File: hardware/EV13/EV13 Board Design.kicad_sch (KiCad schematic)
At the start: 142 parts, among them CN2 Conn_05x02_Female, CN3 Conn_01x06_Female, CN4 Conn_01x06_Female, CN5 Conn_02x05_Male, CN6 Conn_02x05_Male, CN7 Conn_02x05_Male, J1 Conn_01x02_Socket, J10 Conn_01x08_Socket, J2 AudioJack1, J3 Conn_01x06_Socket, J9 USB_C_Receptacle, SW1 TS-1037-A11B3-D2, SW3 TS-1037-A11B3-D2, SW4 SW_Push, SW5 SW_Push, SW6 SW_SPDT, U1 STM32F405RGTx, U11 ESP32-S3-WROOM-1-N8R2, U13 BM14B(0.8)-24DS-0.4V(53), U2 BQ21040DBV, U3 CH340C, U4 USBLC6-2P6, U5 M24C02-RMN6TP, U6 WM8960CGEFL/RV, U7 TPS63060, U8 STM32F072CBTx, Y1 Crystal_GND24

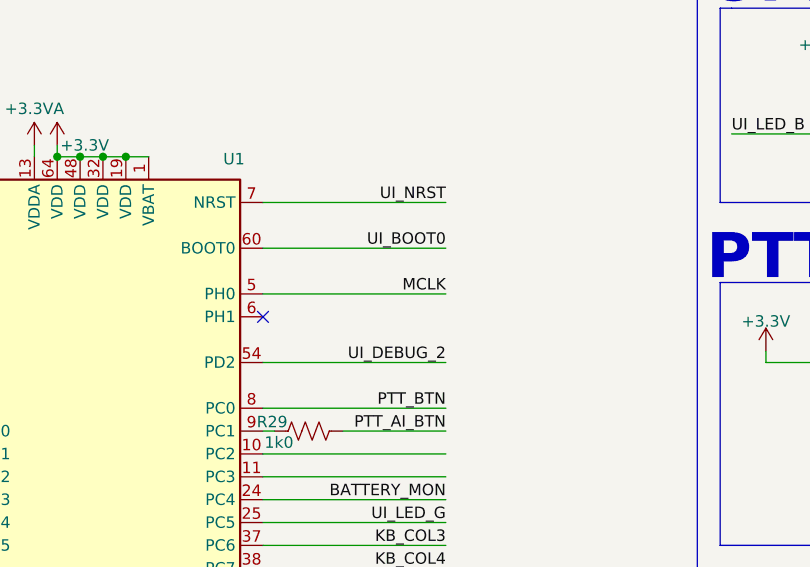
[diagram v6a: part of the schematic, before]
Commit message: feat(sch): Added pulldown resistor to ui_boot0
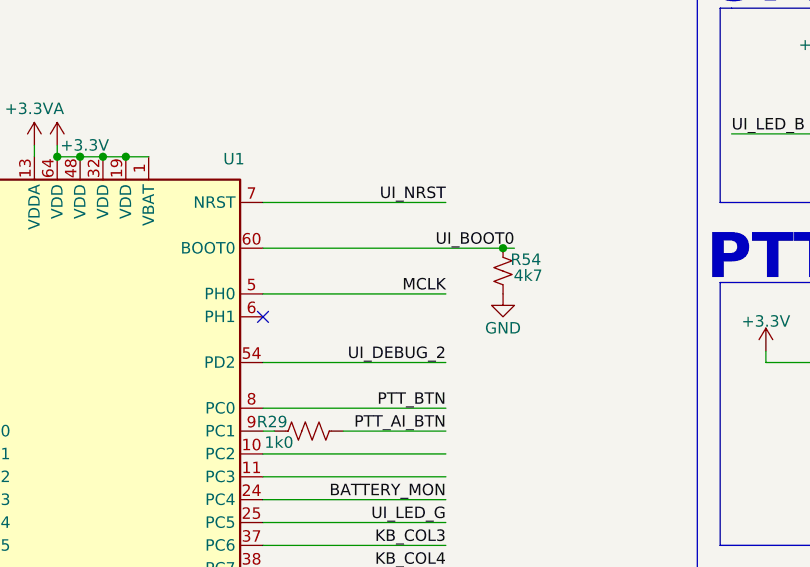
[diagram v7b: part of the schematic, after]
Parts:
- added R54: 4k7, Resistor_SMD:R_0402_1005Metric, symbol Device:R_Small_US
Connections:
- net GND: now also R54.2
- net UI_BOOT0: now also R54.1
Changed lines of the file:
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@@
 	)
 	(junction
+		(at 422.91 96.52)
+		(diameter 0)
+		(color 0 0 0 0)
+	)
+	(junction
 		(at 64.77 370.84)
 		(diameter 0)
@@
 	(wire
 		(pts
-			(xy 396.24 96.52) (xy 416.56 96.52)
+			(xy 396.24 96.52) (xy 422.91 96.52)
 		)
 		(stroke
@@
 	(wire
 		(pts
+			(xy 422.91 96.52) (xy 424.18 96.52)
+		)
+		(stroke
+			(width 0)
+			(type default)
+		)
+	)
+	(wire
+		(pts
 			(xy 494.03 78.74) (xy 504.19 78.74)
 		)
@@
 	)
 	(label "UI_BOOT0"
-		(at 416.56 96.52 180)
+		(at 424.18 96.52 180)
 		(effects
 			(font
@@
 	)
 	(symbol
+		(lib_id "power:GND")
+		(at 422.91 101.6 0)
+		(unit 1)
+		(exclude_from_sim no)
+		(in_bom yes)
+		(on_board yes)
+		(dnp no)
+		(property "Reference" "#PWR29"
+			(at 422.91 107.95 0)
+			(effects
+				(font
+					(size 1.27 1.27)
+				)
+				(hide yes)
+			)
+		)
+		(property "Value" "GND"
+			(at 422.91 105.41 0)
+			(effects
+				(font
+					(size 1.27 1.27)
+				)
+			)
+		)
+		(property "Footprint" ""
+			(at 422.91 101.6 0)
+			(effects
+				(font
+					(size 1.27 1.27)
+				)
+				(hide yes)
+			)
+		)
+		(property "Datasheet" ""
+			(at 422.91 101.6 0)
+			(effects
+				(font
+					(size 1.27 1.27)
+				)
+				(hide yes)
+			)
+		)
+		(property "Description" "Power symbol creates a global label with name \"GND\" , ground"
+			(at 422.91 101.6 0)
+			(effects
+				(font
+					(size 1.27 1.27)
+				)
+				(hide yes)
+			)
+		)
+		(pin "1"
+		)
+		(instances
+			(project "EV13 Board Design"
+				(path "/bd865368-262b-4f76-b7a6-1673c2cb0f8c"
+					(reference "#PWR29")
+					(unit 1)
+				)
+			)
+		)
+	)
+	(symbol
 		(lib_id "power:+3.3VA")
 		(at 370.84 85.09 0)
@@
 					(unit 1)
 				)
+			)
+		)
+	)
+	(symbol
+		(lib_id "Device:R_Small_US")
+		(at 422.91 99.06 0)
+		(unit 1)
+		(exclude_from_sim no)
+		(in_bom yes)
+		(on_board yes)
+		(dnp no)
+		(property "Reference" "R54"
+			(at 425.45 97.79 0)
+			(effects
+				(font
+					(size 1.27 1.27)
+				)
+			)
+		)
+		(property "Value" "4k7"
+			(at 425.704 99.568 0)
+			(effects
+				(font
+					(size 1.27 1.27)
+				)
+			)
+		)
+		(property "Footprint" "Resistor_SMD:R_0402_1005Metric"
+			(at 422.91 99.06 0)
+			(effects
+				(font
+					(size 1.27 1.27)
+				)
+				(hide yes)
+			)
+		)
+		(property "Datasheet" "~"
+			(at 422.91 99.06 0)
+			(effects
+				(font
+					(size 1.27 1.27)
+				)
+				(hide yes)
+			)
+		)
+		(property "Description" "Resistor, small US symbol"
+			(at 422.91 99.06 0)
+			(effects
+				(font
+					(size 1.27 1.27)
+				)
+				(hide yes)
+			)
+		)
+		(property "JLCPCB Part #" "C25900"
+			(at 422.91 99.06 0)
+			(effects
+				(font
+					(size 1.27 1.27)
+				)
+				(hide yes)
+			)
+		)
+		(pin "1"
+		)
+		(pin "2"
+		)
+		(instances
+			(project "EV13 Board Design"
+				(path "/bd865368-262b-4f76-b7a6-1673c2cb0f8c"
+					(reference "R54")
+					(unit 1)
+				)

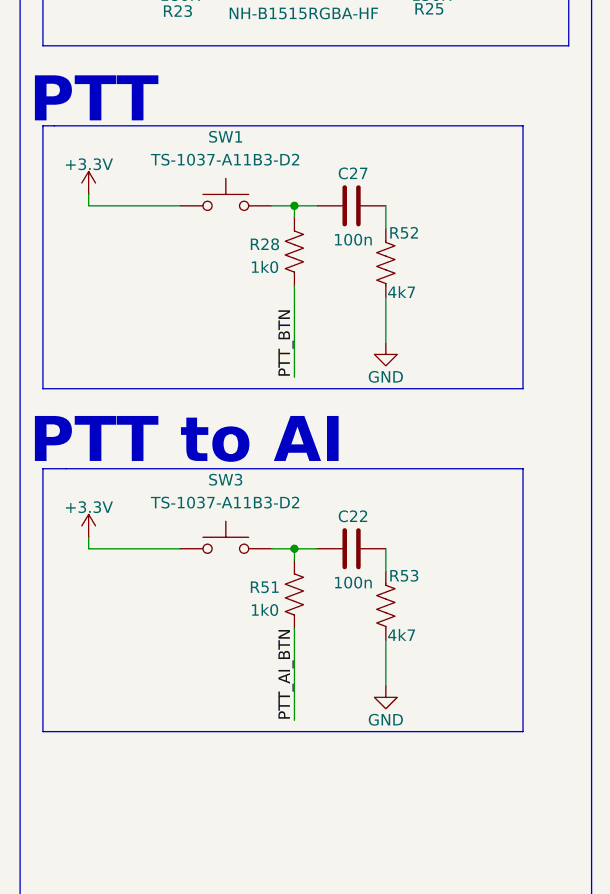
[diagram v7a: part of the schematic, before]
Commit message: chore(sch): Fix rc filter on ptt
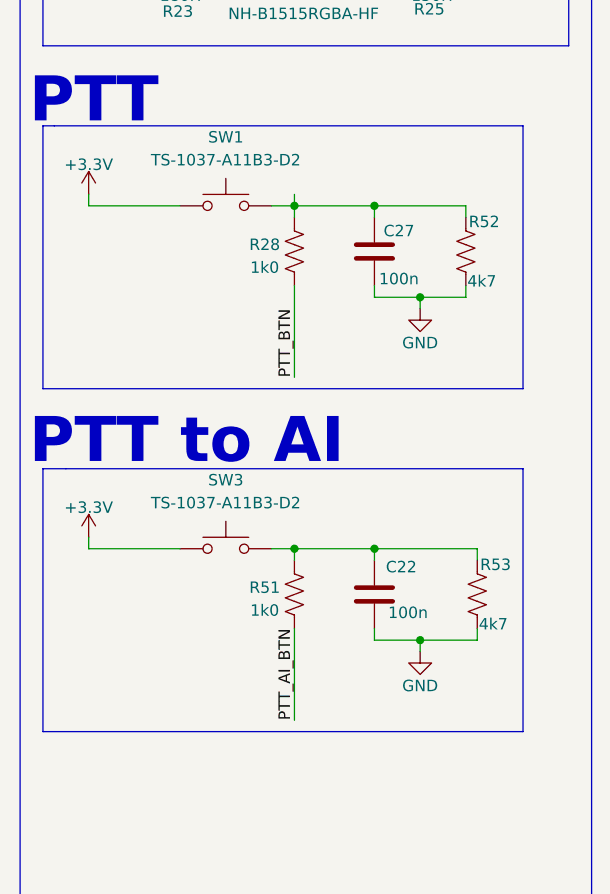
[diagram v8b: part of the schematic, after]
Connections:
- net GND: now also C22.2, C27.2
- net at R28.2, SW1.2: now also C27.1, R52.2; no longer C27.2
- net at R51.2, SW3.2: now also C22.1, R53.2; no longer C22.2
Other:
- moved on the sheet: C22, C27, R52, R53
